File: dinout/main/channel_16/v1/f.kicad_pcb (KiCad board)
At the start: 2 copper layers, 76.8 x 81.3 mm, 29 parts, among them J1 fm16_i, J10 8, J11 wrs_i, J12 selector4_i, J13 bus_i, J14 9, J15 10, J16 11, J17 12, J18 13, J19 14, J2 0, J20 15, J21 data_manager_i, J22 data_manager_i, J23 wrs_i, J24 S0, J25 S1, J3 1, J4 2, J5 3, J6 4, J7 5, J8 6, J9 7

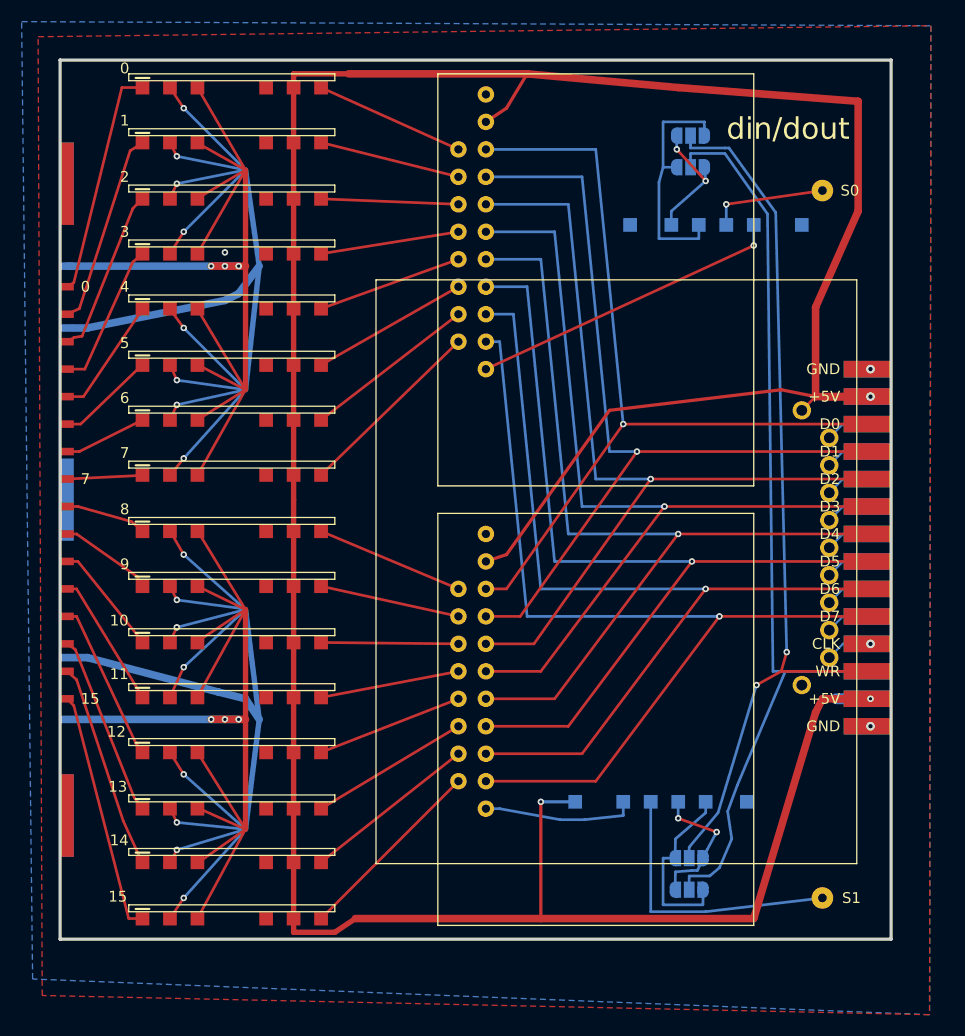
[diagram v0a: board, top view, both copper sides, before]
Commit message: voltage regulator for each module
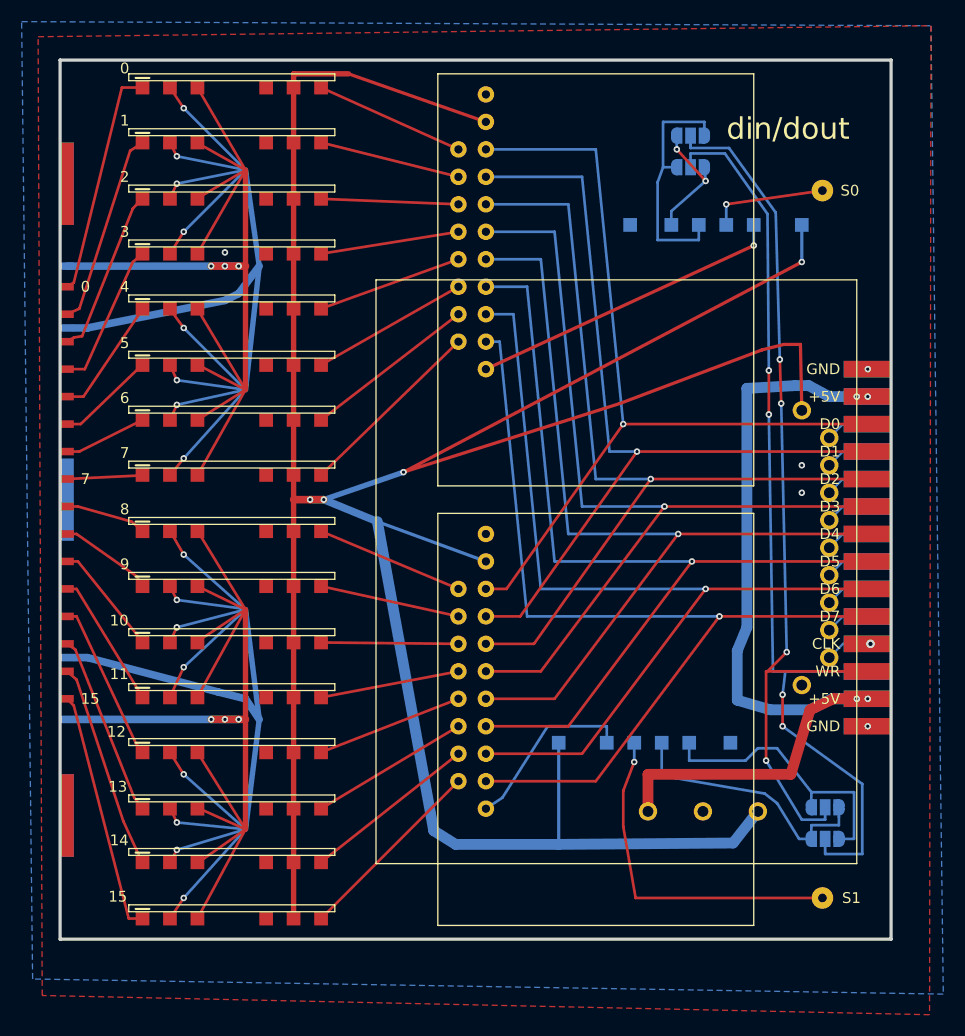
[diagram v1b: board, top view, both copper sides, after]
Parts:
- added J26: power_+5V, plc88:power_i, B.Cu at (3.56, 73.3)
- moved JP3 13.4 mm to (26.3, 62.7)
- moved JP4 13.4 mm to (26.3, 65.7)
- moved J23 5.67 mm to (10.5, 54.2)
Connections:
- J13 pad 25: +5V -> VPBUS
- J13 pad 26: +5V -> VPBUS
- J13 pad 3: +5V -> VPBUS
- J13 pad 4: +5V -> VPBUS
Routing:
- net VPBUS: track 0.00 -> 81.3 mm, vias 0 -> 4
- net +5V: track 304.3 -> 284.6 mm, vias 3 -> 4
- net YES8_15: track 13.0 -> 24.6 mm, vias 2 -> 0
- net NO8_15: track 17.0 -> 26.4 mm
- net S1: track 26.1 -> 31.9 mm, vias 0 -> 1
- net SW1: track 14.1 -> 16.6 mm
- net RD: track 85.9 -> 87.6 mm, vias 0 -> 4
- net WR: track 82.7 -> 82.6 mm, vias 2 -> 4
- net GND: vias 3 -> 5
